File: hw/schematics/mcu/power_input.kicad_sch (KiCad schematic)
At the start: 26 parts

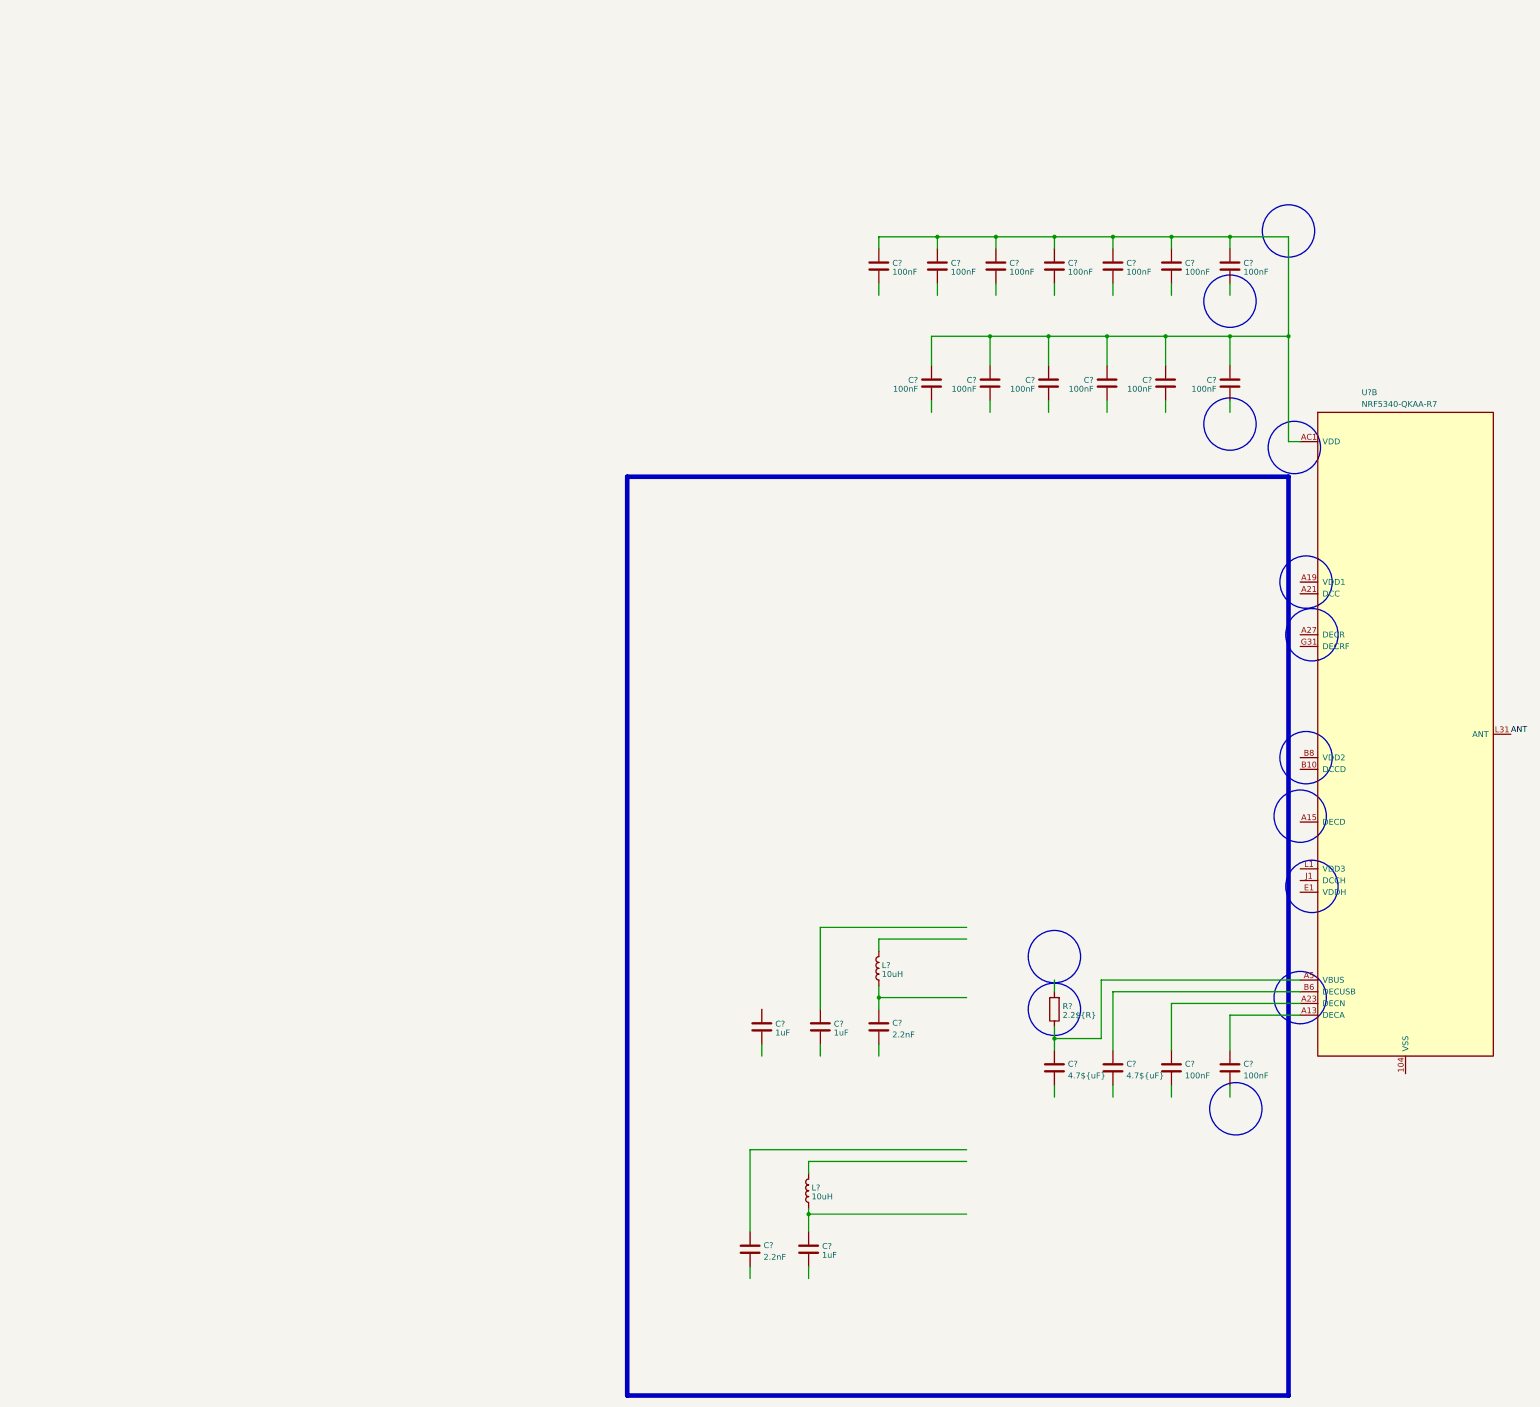
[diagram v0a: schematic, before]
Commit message: 
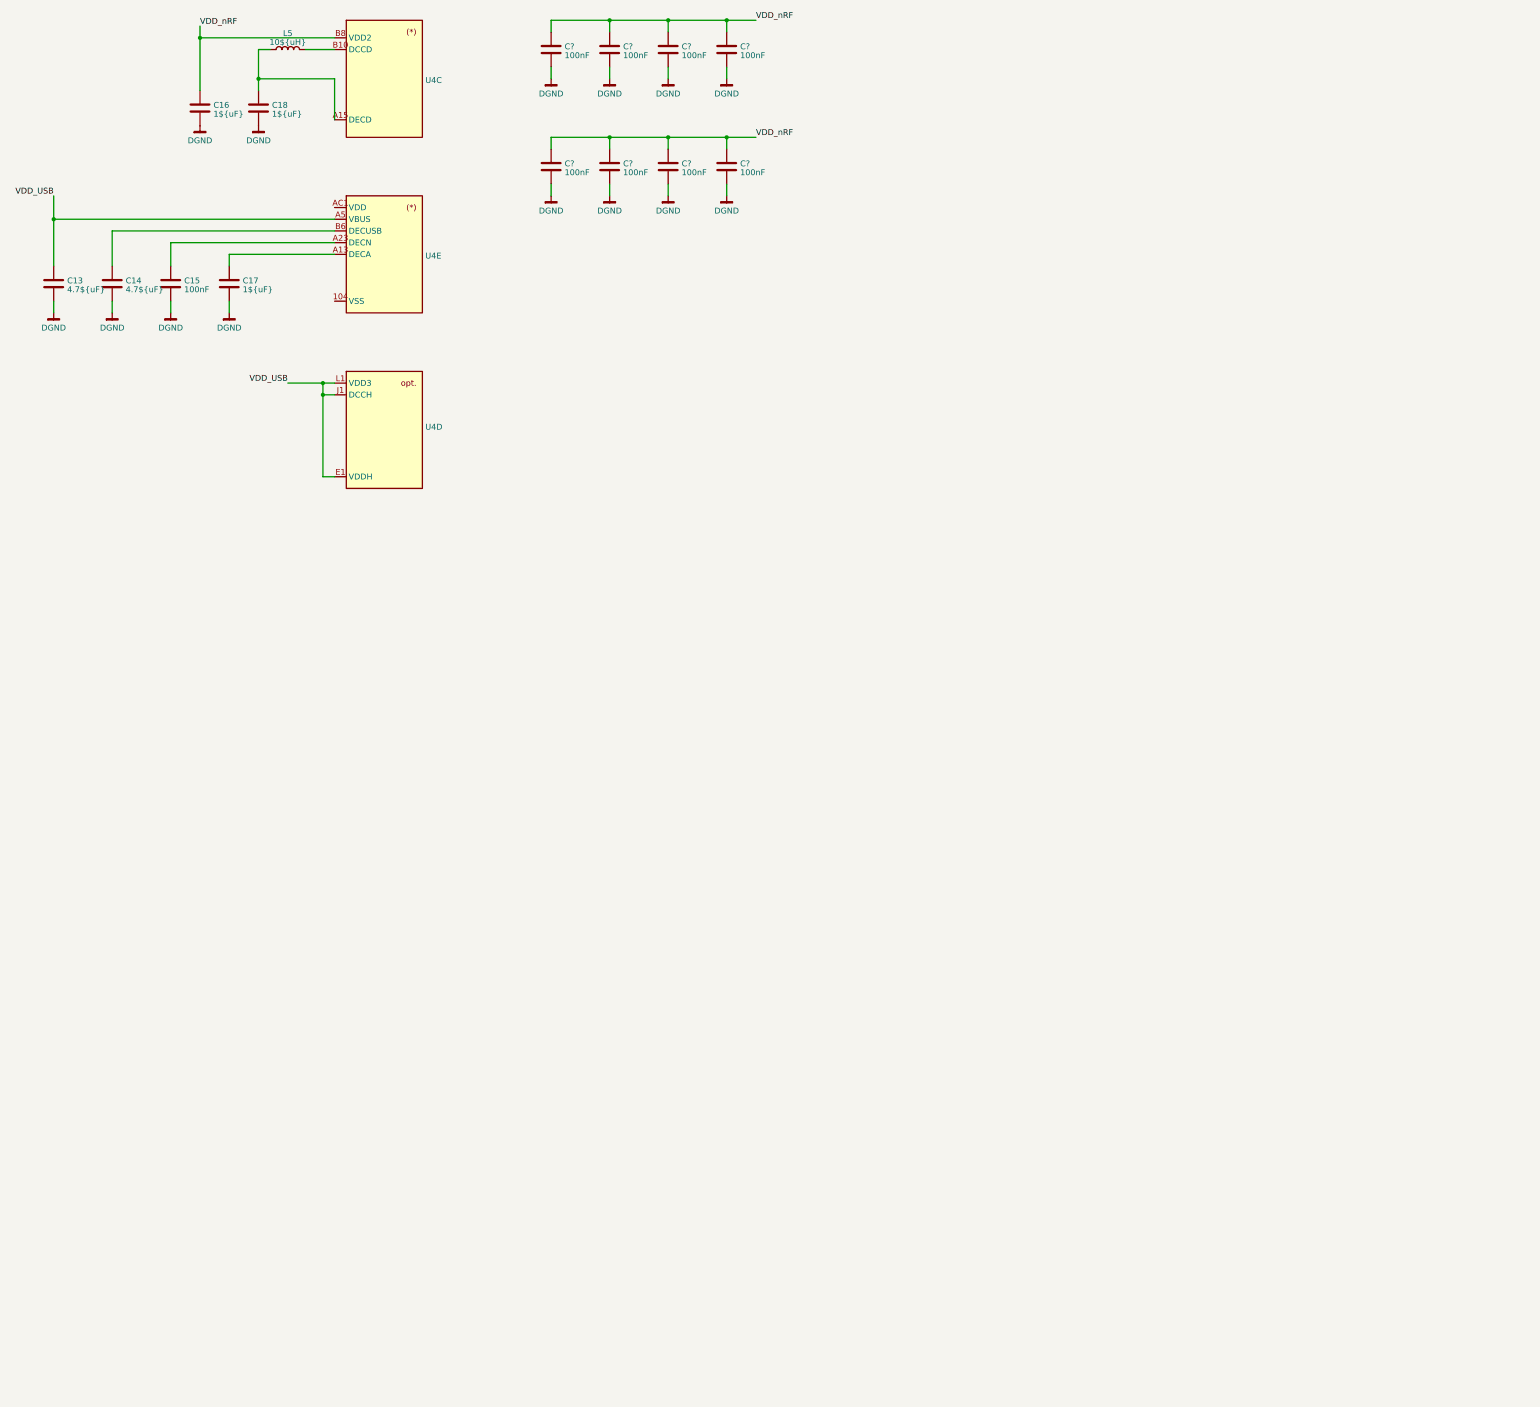
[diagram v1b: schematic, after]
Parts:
- removed C? (x7): 100nF, Capacitor_SMD:C_0201_0603Metric, symbol Device:C
- removed C? (x3): 1uF, Capacitor_SMD:C_0402_1005Metric, symbol Device:C
- removed C? (x2): 2.2nF, Capacitor_SMD:C_0201_0603Metric, symbol Device:C
- removed C? (x2): 4.7${uF}, Capacitor_SMD:C_0402_1005Metric, symbol Device:C
- removed L? (x2): 10uH, Inductor_SMD:L_0603_1608Metric, symbol Device:L
- removed R?: 2.2${R}, Resistor_SMD:R_0402_1005Metric, symbol Device:R
- removed U?: NRF5340-QKAA-R7, 0:NRF5340-QKAA-R7, symbol 1.Embedded.Specialized:NRF5340-QKAA-R7
- added C13, C14: 4.7${uF}, symbol Device:C
- added C15: 100nF, symbol Device:C
- added C16, C17, C18: 1${uF}, symbol Device:C
- added L5: 10${uH}, symbol Device:L
- added U4: NRF5340-QKAA-R7, 0:NRF5340-QKAA-R7, symbol 1.Embedded.Specialized:NRF5340-QKAA-R7
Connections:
- net VDD: now also U4.AC1 (VDD), U4.AG1 (VDD), U4.AJ31 (VDD), U4.AL11 (VDD), U4.AL17 (VDD), U4.AL25 (VDD), U4.AL3 (VDD), U4.AL7 (VDD), U4.B28 (VDD), U4.C1 (VDD), U4.E31 (VDD), U4.N31 (VDD), U4.U1 (VDD); no longer C?.1, C?.1, C?.1, C?.1, C?.1, C?.1, C?.1, C?.1
- net VSS: now also U4.104 (VSS), U4.35 (VSS), U4.36 (VSS), U4.37 (VSS), U4.38 (VSS), U4.39 (VSS), U4.40 (VSS), U4.41 (VSS), U4.43 (VSS), U4.44 (VSS), U4.45 (VSS), U4.46 (VSS), U4.47 (VSS), U4.48 (VSS), U4.49 (VSS), U4.50 (VSS), U4.51 (VSS), U4.A25 (VSS), U4.B12 (VSS), U4.B26 (VSS), U4.G1 (VSS), U4.H2 (VSS), U4.J31 (VSS)
- net DGND: now reaches C?.2
- net DGND: now also C?.2, C?.2, C?.2, C?.2, C?.2, C?.2, C?.2, C13.2, C14.2, C15.2, C16.2, C17.2, C18.2
- new net: C14.1, U4.B6 (DECUSB)
- new net: C18.1, L5.1, U4.A15 (DECD)
- new net: L5.2, U4.B10 (DCCD)
- new net: C17.1, U4.A13 (DECA)
- new net: C15.1, U4.A23 (DECN)
- new net VDD_USB: C13.1, U4.A5 (VBUS), U4.E1 (VDDH), U4.J1 (DCCH), U4.L1 (VDD3)
- new net VDD_nRF: C16.1, C?.1, C?.1, C?.1, C?.1, C?.1, C?.1, C?.1, C?.1, U4.B8 (VDD2)
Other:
- moved on the sheet: C?
